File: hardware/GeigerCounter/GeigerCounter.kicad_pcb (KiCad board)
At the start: 2 copper layers, 20 parts, among them Q1 MMBTA44, Q2 MMBTA44, Q3 MMBT3904, U1 NE555D

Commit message: work with kicad
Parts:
- added J4: GameBoy_GamePak_DMG-09, SI3BG:Gameboy-Connector, F.Cu at (218.4, 134.2)
- R6: footprint Resistor_SMD:R_0805_2012Metric_Pad1.20x1.40mm_HandSolder -> Resistor_SMD:R_2010_5025Metric_Pad1.40x2.65mm_HandSolder
- moved R7 124.9 mm to (232.1, 110.1), turned to 180 degrees
- moved R8 120.4 mm to (231.1, 102.3), turned to 180 degrees
- moved R9 118.9 mm to (231.1, 100.1)
- moved R1 116.2 mm to (226.6, 85.1), turned to 180 degrees
- moved R2 116.0 mm to (225.5, 90.6), turned to 90 degrees
- moved R4 114.4 mm to (226.6, 87.5)
- moved Q3 105.6 mm to (231.1, 105.6), turned to -90 degrees
- moved R3 104.8 mm to (216.9, 83.8)
- moved C1 92.9 mm to (228.9, 91.6), turned to 180 degrees
- moved C3 92.8 mm to (226.6, 100.1), turned to 180 degrees
- moved D1 87.6 mm to (229.9, 88.4), turned to 90 degrees
- moved U1 85.6 mm to (220.1, 88.5), turned to 180 degrees
- moved R5 85.1 mm to (223.6, 81.0)
- moved Q2 85.0 mm to (217.2, 80.9)
- moved L1 83.9 mm to (202.6, 89.6), turned to 90 degrees
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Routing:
- net /CARD_A14: track 0.00 -> 16.5 mm, vias 0 -> 2
- net Net-(Q1-B): track 0.00 -> 13.6 mm
- net Net-(D2-A): track 0.00 -> 13.0 mm
- net Net-(Q2-C): track 0.00 -> 10.8 mm
- net Net-(Q1-E): track 0.00 -> 10.4 mm
- net Net-(U1-Q): track 0.00 -> 9.51 mm
- net Net-(D1-A): track 0.00 -> 8.40 mm
- net Net-(R6-Pad2): track 0.00 -> 8.10 mm
- net Net-(D2-K): track 0.00 -> 7.05 mm
- net GND: track 0.00 -> 6.98 mm, vias 0 -> 29
- net Net-(Q3-B): track 0.00 -> 4.55 mm
- net /INT: track 0.00 -> 3.60 mm
- net Net-(C3-Pad1): track 0.00 -> 2.42 mm
- net Net-(D1-K): track 0.00 -> 2.18 mm
- added copper zone on B.Cu, net GND
- added copper zone on F.Cu, net GND
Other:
- board outline added: 51 x 90.6 mm
- board text added: "2 5"
- board text added: "3 9"
- board text added: "PCB Thickness: 0.8mm!!"
- board text added: "jsc69@gmx.de"

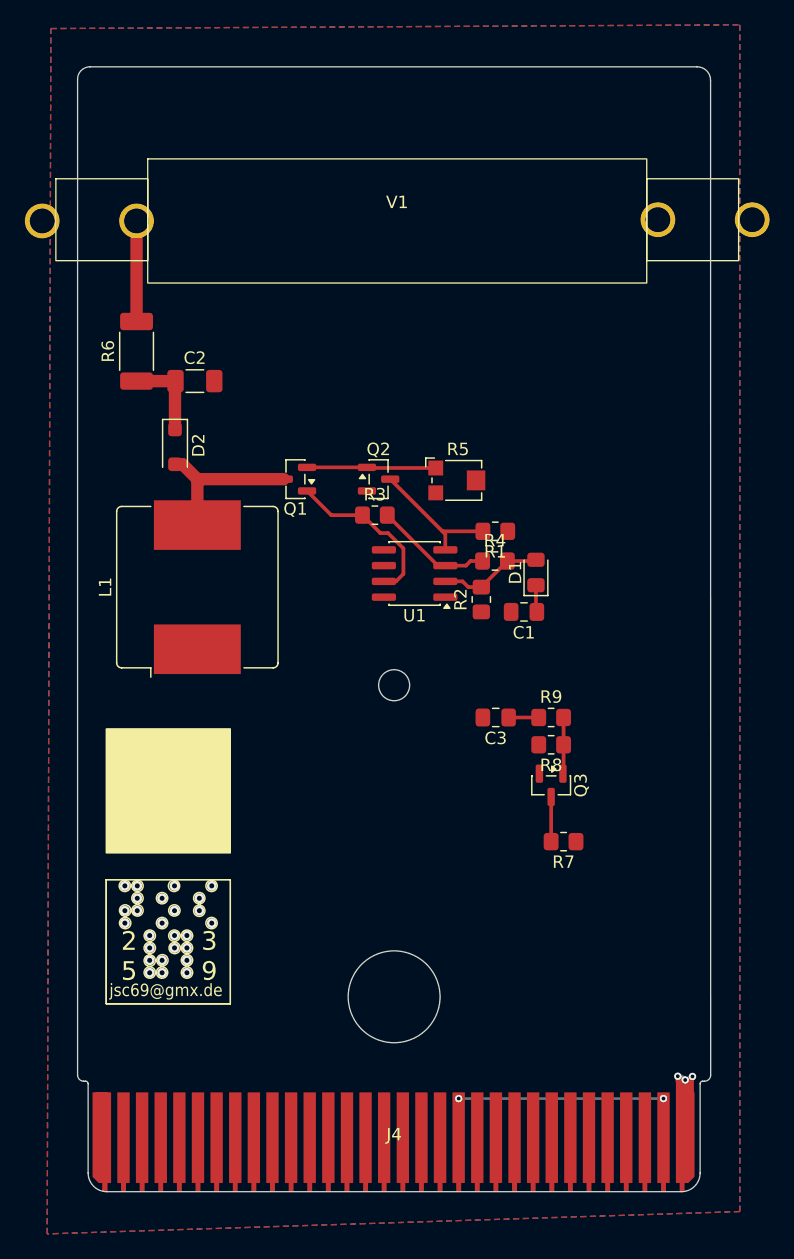
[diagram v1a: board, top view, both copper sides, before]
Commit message: change to 2 inductors
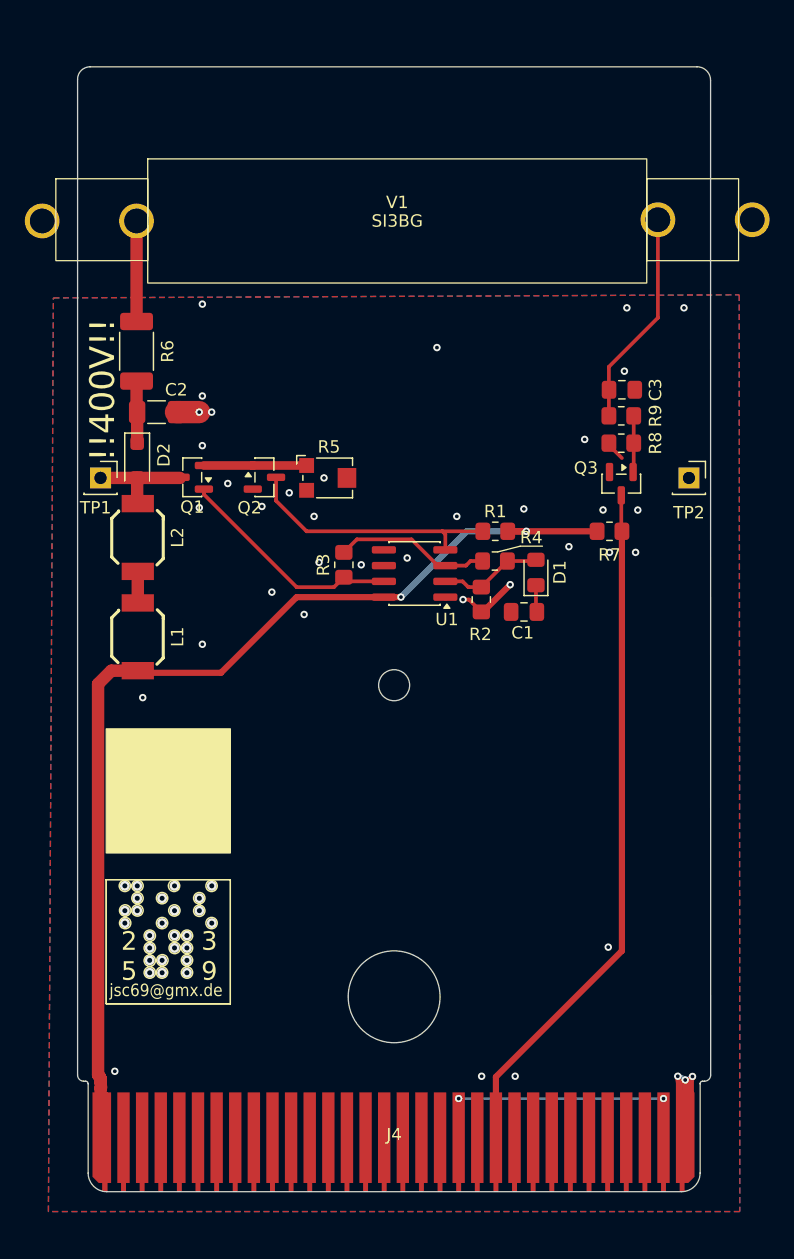
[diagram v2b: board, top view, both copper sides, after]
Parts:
- added L2: 4.7mH, EasyEDA:IND-SMD_L6.6-W4.4, F.Cu at (197.8, 85.6)
- added TP1: TestPoint, Connector_PinSocket_2.54mm:PinSocket_1x01_P2.54mm_Vertical, F.Cu at (194.8, 80.8)
- added TP2: TestPoint, Connector_PinSocket_2.54mm:PinSocket_1x01_P2.54mm_Vertical, F.Cu at (242.2, 80.8)
- L1: value 10mH -> 4.7mH; footprint Inductor_SMD:L_Bourns_SRR1208_12.7x12.7mm -> EasyEDA:IND-SMD_L6.6-W4.4
- moved C3 28.3 mm to (236.8, 73.7), turned to 0 degrees
- moved R7 25.3 mm to (235.8, 85.1), turned to 0 degrees
- moved Q3 24.9 mm to (236.8, 81.3)
- moved R8 24.9 mm to (236.8, 78.0)
- moved R9 24.9 mm to (236.8, 75.8)
- moved R5 10.4 mm to (213.2, 80.8)
- moved Q2 9.20 mm to (208.0, 80.8)
- moved Q1 8.31 mm to (202.2, 80.8)
- moved L1 6.25 mm to (197.8, 93.6), turned to -90 degrees
- moved R3 4.72 mm to (214.4, 87.8), turned to 90 degrees
- moved C2 3.97 mm to (199.3, 75.5)
- moved D2 3.24 mm to (197.8, 79.4)
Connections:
- L1 pad 1: VCC -> +5V
- L1 pad 2: Net-(D2-A) -> Net-(L1-Pad2)
- Q3 pad 3: /INT -> /CARD_D0
- R1 pad 1: VCC -> +5V
- R7 pad 1: VCC -> +5V
- R7 pad 2: /INT -> /CARD_D0
- U1 pad 8: VCC -> +5V
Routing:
- net +5V: track 0.00 -> 82.0 mm, vias 0 -> 2
- net /CARD_D0: track 0.00 -> 52.8 mm
- net Net-(C3-Pad1): track 2.42 -> 17.4 mm
- net Net-(Q2-C): track 10.8 -> 21.2 mm
- net GND: track 6.98 -> 15.8 mm, vias 29 -> 65
- net Net-(Q1-B): track 13.6 -> 18.5 mm
- net Net-(D2-A): track 13.0 -> 8.60 mm
- net /INT: track 3.60 -> 0.00 mm
- net Net-(U1-Q): track 9.51 -> 12.6 mm
- net Net-(L1-Pad2): track 0.00 -> 2.54 mm
- net Net-(Q1-E): track 10.4 -> 8.28 mm
- net Net-(D2-K): track 7.05 -> 5.02 mm
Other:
- board text added: "!!400V!!"
- board text added: "Leiterbahn: Empfohlen: 0.5 mm - 1.0 mm Breite für die 400V-Leitungen. Vermeide scharfe Ecken (runde oder abgeschrägte Ecken sind besser). Bauteile: 1210 für R & C (wegen Spannungsfestigkeit), SMA-Diode (1000V). Abstände (Clearance): 1.5 - 2.0 mm zwischen allen 400V-Leitern und zu GND. Keine {dblquote}Backplane{dblquote} mit GND"
